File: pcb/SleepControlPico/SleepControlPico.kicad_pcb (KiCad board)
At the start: 2 copper layers, 74.4 x 49.3 mm, 24 parts, among them J1 USB_C_Receptacle_PowerOnly_6P, J3 UART, J4 FFC2B35-18-G_REVA2, SW1 RotaryEncoder_Switch, SW2 SW_Push, U1 AMS1117-33, U2 ESP32-WROOM-32D, U3 LIS3DH

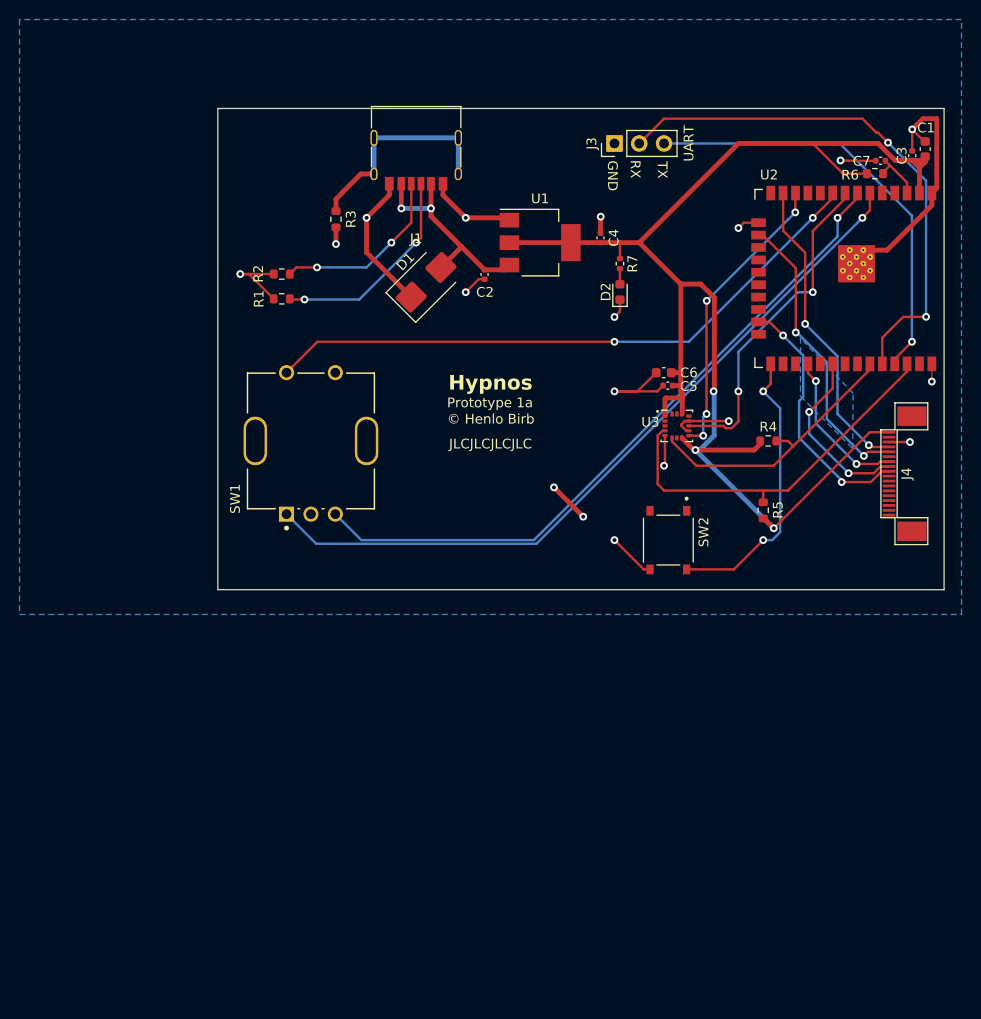
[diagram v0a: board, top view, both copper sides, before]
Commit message: Smaller PCB using an ESP32-S3-MINI-1.
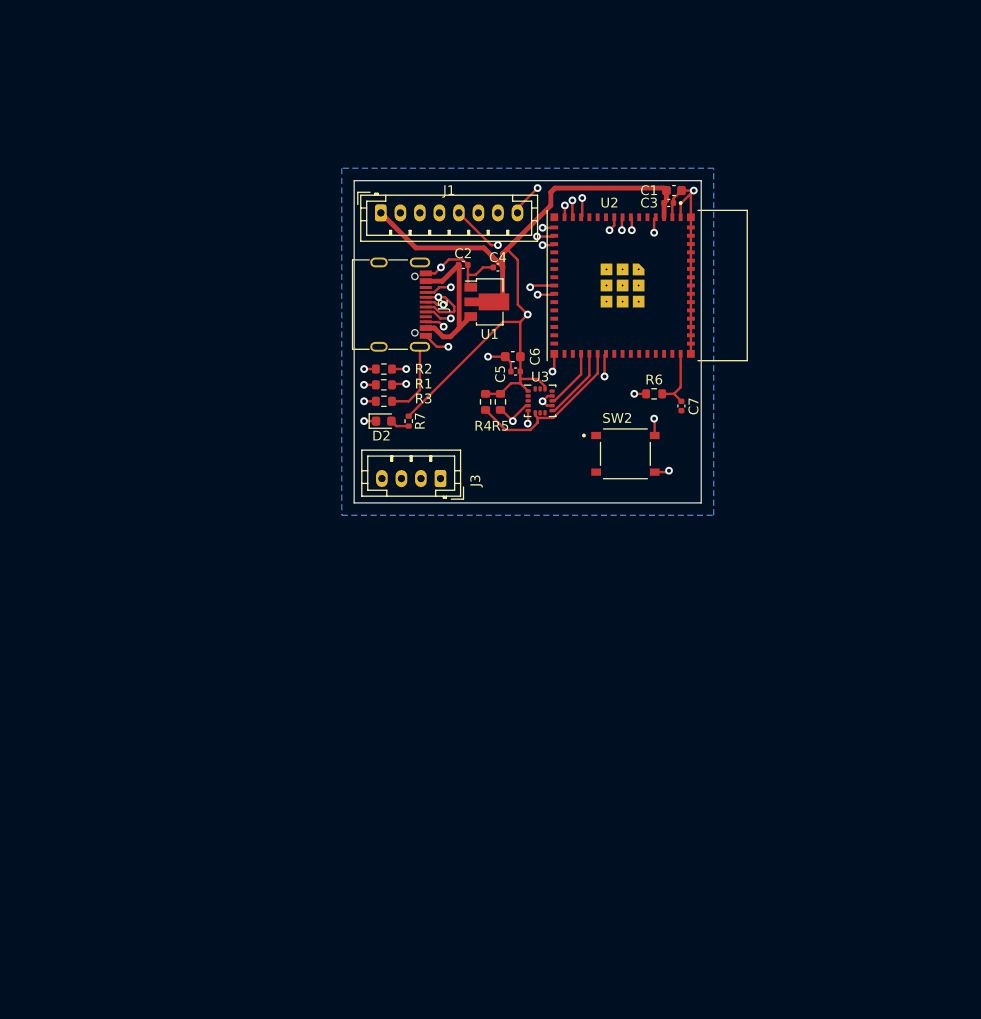
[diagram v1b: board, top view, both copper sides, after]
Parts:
- removed D1: SMBJ6.0A, Diode_SMD:D_SMB
- removed J4: FFC2B35-18-G_REVA2, Connector_FFC-FPC:Jushuo_AFC07_S18FCC
- removed SW1: RotaryEncoder_Switch, eec:Bourns-PEC11R-4020F-S0012-MFG
- added J2: USB_C_Receptacle_USB2.0, Connector_USB:USB_C_Receptacle_G-Switch_GT-USB-7010ASV, F.Cu at (116.6, 64.8)
- J1: value USB_C_Receptacle_PowerOnly_6P -> Conn_01x08_Pin; footprint Connector_USB:USB_C_Receptacle_G-Switch_GT-USB-7002C -> Connector_JST:JST_PH_B8B-PH-K_1x08_P2.00mm_Vertical
- J3: value UART -> Conn_01x04_Socket; footprint Connector_PinHeader_2.54mm:PinHeader_1x03_P2.54mm_Vertical -> Connector_JST:JST_PH_B4B-PH-K_1x04_P2.00mm_Vertical
- U1: footprint Package_TO_SOT_SMD:SOT-223-3_TabPin2 -> Package_TO_SOT_SMD:SOT-89-3
- U2: value ESP32-WROOM-32D -> ESP32-S3-MINI-1-N8; footprint RF_Module:ESP32-WROOM-32D -> ESP32-S3-MINI-1-N8:XCVR_ESP32-S3-MINI-1-N8
- moved J3 38.7 mm to (121.9, 82.6), turned to 180 degrees
- moved C7 32.4 mm to (146.6, 75.2), turned to 90 degrees
- moved R6 32.0 mm to (143.8, 73.9)
- moved R4 29.2 mm to (126.5, 74.7), turned to -90 degrees
- moved R5 29.1 mm to (128.0, 74.7), turned to 90 degrees
- moved D2 27.6 mm to (116.1, 76.7), turned to 0 degrees
- moved R7 27.0 mm to (118.6, 76.7)
- moved C1 26.1 mm to (145.8, 53.1), turned to 0 degrees
- moved C3 25.4 mm to (145.3, 54.4), turned to 0 degrees
- moved U2 23.5 mm to (140.5, 62.8)
- moved R3 19.3 mm to (116.1, 74.7), turned to 180 degrees
- moved C5 15.7 mm to (129.6, 71.6)
- moved C6 15.5 mm to (129.3, 70.1)
- moved R2 14.3 mm to (116.1, 71.4)
- moved U3 14.2 mm to (132.1, 74.6)
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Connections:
- R1 pad 1: Net-(J1-CC1) -> Net-(J2-CC1)
- R2 pad 1: Net-(J1-CC2) -> Net-(J2-CC2)
- R3 pad 1: Net-(J1-SHIELD) -> Net-(J2-SHIELD)
- R4 pad 2: Net-(U2-IO21) -> Net-(U2-IO39)
- U2 pad 12: Net-(U2-IO27) -> unconnected-(U2-IO8-Pad12)
- U2 pad 13: Net-(J4-SCK) -> /Disp_LITE
- U2 pad 14: unconnected-(U2-IO12-Pad14) -> /Disp_RST
- U2 pad 15: GND -> /Disp_MOSI
- U2 pad 16: Net-(J4-MOSI) -> /Disp_SCLK
- U2 pad 17: unconnected-(U2-SHD/SD2-Pad17) -> /Disp_CS
- U2 pad 18: unconnected-(U2-SWP/SD3-Pad18) -> /Disp_DC
- U2 pad 2: +3.3V -> GND
- U2 pad 24: unconnected-(U2-IO2-Pad24) -> Net-(U2-IO20)
- U2 pad 25: Net-(U2-IO0) -> unconnected-(U2-IO21-Pad25)
- U2 pad 28: Net-(J4-DC) -> unconnected-(U2-IO33-Pad28)
- U2 pad 3: Net-(U2-EN) -> +3.3V
- U2 pad 30: Net-(J4-RST) -> unconnected-(U2-IO48-Pad30)
- U2 pad 33: Net-(U2-IO21) -> Net-(U2-IO37)
- U2 pad 34: Net-(J3-Pin_2) -> Net-(U2-IO38)
- U2 pad 35: Net-(J3-Pin_3) -> Net-(U2-IO39)
- U2 pad 38: GND -> unconnected-(U2-IO42-Pad38)
- U2 pad 39: GND -> unconnected-(U2-TXD0-Pad39)
- U2 pad 4: unconnected-(U2-SENSOR_VP-Pad4) -> Net-(U2-IO0)
- U2 pad 6: Net-(U2-IO34) -> unconnected-(U2-IO2-Pad6)
- U2 pad 7: Net-(U2-IO35) -> Net-(J3-Pin_2)
- U2 pad 8: Net-(U2-IO32) -> Net-(J3-Pin_3)
- U2 pad 9: Net-(U2-IO33) -> Net-(J3-Pin_4)
- U3 pad 11: Net-(U2-IO32) -> Net-(U2-IO37)
- U3 pad 6: Net-(U2-IO21) -> Net-(U2-IO39)
- U3 pad 8: +3.3V -> unconnected-(U3-CS-Pad8)
- U3 pad 9: Net-(U2-IO27) -> Net-(U2-IO38)
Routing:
- net Net-(U2-IO34): track 77.0 -> 0.00 mm, vias 1 -> 0
- net Net-(U2-IO35): track 70.7 -> 0.00 mm, vias 1 -> 0
- net Net-(U2-IO33): track 63.9 -> 0.00 mm, vias 2 -> 0
- net GND: track 102.2 -> 53.2 mm, vias 18 -> 12
- net +3.3V: track 145.0 -> 101.4 mm, vias 3 -> 2
- net Net-(J3-Pin_4): track 0.00 -> 36.9 mm, vias 0 -> 1
- net Net-(U2-IO32): track 34.3 -> 0.00 mm, vias 2 -> 0
- net Net-(J4-SCK): track 31.6 -> 0.00 mm, vias 2 -> 0
- net Net-(J4-MOSI): track 30.5 -> 0.00 mm, vias 2 -> 0
- net Net-(U2-IO27): track 30.3 -> 0.00 mm, vias 4 -> 0
- net Net-(U2-IO21): track 28.3 -> 0.00 mm
- net Net-(J2-SHIELD): track 0.00 -> 24.8 mm
- net Net-(J1-SHIELD): track 22.3 -> 0.00 mm
- net Net-(J1-CC1): track 21.6 -> 0.00 mm, vias 2 -> 0
- net Net-(U2-IO40): track 38.8 -> 19.2 mm, vias 0 -> 2
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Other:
- board size 74.4 x 49.3 mm -> 35.6 x 33 mm
- copper layers 2 -> 4
- board text removed: "GND"
- board text removed: "Hypnos"
- board text removed: "JLCJLCJLCJLC"
- board text removed: "Prototype 1a"
- board text removed: "RX"
- board text removed: "TX"
- board text removed: "© Henlo Birb"

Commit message: Final-ish PCB layout
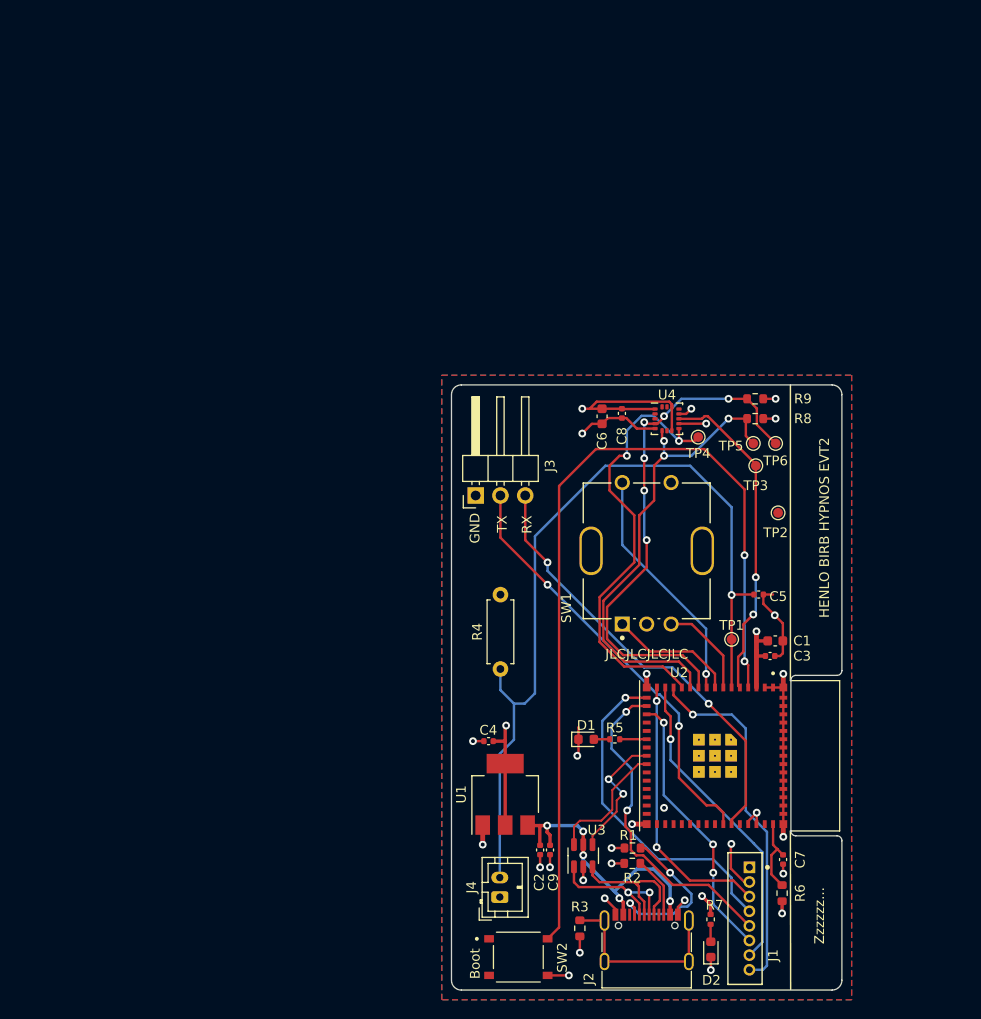
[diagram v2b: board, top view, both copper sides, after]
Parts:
- added C8: 0.1 µF, Capacitor_SMD:C_0402_1005Metric, F.Cu at (140.5, 75.9)
- added C9: 100 nF, Capacitor_SMD:C_0402_1005Metric, F.Cu at (133.1, 120.7)
- added D1: LED, LED_SMD:LED_0603_1608Metric, F.Cu at (136.8, 109.3)
- added J4: Photodiode, Connector_JST:JST_PH_B2B-PH-K_1x02_P2.00mm_Vertical, F.Cu at (128.0, 125.5)
- added R8: 4K7, Resistor_SMD:R_0603_1608Metric, F.Cu at (154.1, 76.5)
- added R9: 4K7, Resistor_SMD:R_0603_1608Metric, F.Cu at (154.1, 74.4)
- added SW1: RotaryEncoder_Switch, eec:Bourns-PEC11R-4020F-S0012-MFG, F.Cu at (143.0, 90.0)
- added TP1: TestPoint, TestPoint:TestPoint_Pad_D1.0mm, F.Cu at (151.7, 99.1)
- added TP2: TestPoint, TestPoint:TestPoint_Pad_D1.0mm, F.Cu at (156.5, 86.1)
- added TP3: TestPoint, TestPoint:TestPoint_Pad_D1.0mm, F.Cu at (154.2, 81.3)
- added TP4: TestPoint, TestPoint:TestPoint_Pad_D1.0mm, F.Cu at (148.3, 78.3)
- added TP5: TestPoint, TestPoint:TestPoint_Pad_D1.0mm, F.Cu at (153.9, 79.0)
- added TP6: TestPoint, TestPoint:TestPoint_Pad_D1.0mm, F.Cu at (156.2, 79.0)
- added U4: LIS3DH, Package_LGA:LGA-16_3x3mm_P0.5mm_LayoutBorder3x5y, F.Cu at (145.1, 76.5)
- C5: value 0.1 µF -> 100 nF
- J1: value Conn_01x08_Pin -> Display; footprint Connector_JST:JST_PH_B8B-PH-K_1x08_P2.00mm_Vertical -> JST B8B-ZR:JST-B8B-ZR-0
- J3: value Conn_01x04_Socket -> Conn_01x03; footprint Connector_JST:JST_PH_B4B-PH-K_1x04_P2.00mm_Vertical -> Connector_PinHeader_2.54mm:PinHeader_1x03_P2.54mm_Horizontal
- R1, R2: value 5.1K -> 5K1
- R4: value 2.2 kΩ -> 200K; footprint Resistor_SMD:R_0603_1608Metric -> Resistor_THT:R_Axial_DIN0207_L6.3mm_D2.5mm_P7.62mm_Horizontal
- R5: value 2.2 kΩ -> 150R; footprint Resistor_SMD:R_0603_1608Metric -> Resistor_SMD:R_0402_1005Metric
- R6: value 10 kΩ -> 10K
- R7: value 75Ω -> 150R
- SW2: value SW_Push -> Boot
- U1: footprint Package_TO_SOT_SMD:SOT-89-3 -> Package_TO_SOT_SMD:SOT-223-3_TabPin2
- U3: value LIS3DH -> USBLC6-2SC6; footprint Package_LGA:LGA-16_3x3mm_P0.5mm_LayoutBorder3x5y -> Package_TO_SOT_SMD:SOT-23-6
- moved J1 81.4 mm to (153.1, 127.7), turned to -90 degrees
- moved J2 71.3 mm to (143.0, 131.0), turned to 0 degrees
- moved D2 63.7 mm to (149.6, 130.8), turned to 90 degrees
- moved C2 60.5 mm to (132.1, 120.7), turned to -90 degrees
- moved R7 59.7 mm to (149.6, 127.8)
- moved R3 57.6 mm to (136.2, 128.7), turned to -90 degrees
- moved R2 56.7 mm to (141.5, 122.0)
- moved R1 53.9 mm to (141.6, 120.5)
- moved R6 52.8 mm to (156.9, 125.1), turned to 90 degrees
- moved SW2 52.7 mm to (129.8, 131.6)
- moved U1 50.5 mm to (128.5, 115.0), turned to 90 degrees
- moved U2 49.1 mm to (150.0, 111.0)
- moved C4 48.5 mm to (126.8, 109.5)
- moved C7 47.6 mm to (157.0, 121.6)
- moved C3 47.6 mm to (155.6, 100.8)
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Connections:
- net Net-(J2-CC1) renamed /CC1
- net Net-(J2-CC2) renamed /CC2
- net Net-(J2-SHIELD) renamed /SHIELD
- net Net-(U2-EN) renamed /EN
- net Net-(U2-IO0) renamed /BOOT
- C5 pad 1: +3.3V -> GND
- C5 pad 2: GND -> /PD-
- C6 pad 1: +3.3V -> GND
- C6 pad 2: GND -> +3.3V
- J2 pad A6: Net-(U2-IO20) -> /USB_D-
- J2 pad A7: Net-(U2-IO19) -> /USB_D+
- J2 pad B6: Net-(U2-IO20) -> /USB_D-
- J2 pad B7: Net-(U2-IO19) -> /USB_D+
- J3 pad 2: Net-(J3-Pin_2) -> /UART_TX
- J3 pad 3: Net-(J3-Pin_3) -> /UART_RX
- R4 pad 1: +3.3V -> /PD-
- R4 pad 2: Net-(U2-IO39) -> GND
- R5 pad 1: Net-(U2-IO40) -> Net-(D1-A)
- R5 pad 2: +3.3V -> /Status_LED
- U2 pad 10: unconnected-(U2-IO6-Pad10) -> /ACC_SCL
- U2 pad 11: unconnected-(U2-IO7-Pad11) -> /ACC_SDA
- U2 pad 12: unconnected-(U2-IO8-Pad12) -> /ACC_INT2
- U2 pad 21: unconnected-(U2-IO17-Pad21) -> /Status_LED
- U2 pad 33: Net-(U2-IO37) -> unconnected-(U2-IO37-Pad33)
- U2 pad 34: Net-(U2-IO38) -> unconnected-(U2-IO38-Pad34)
- U2 pad 35: Net-(U2-IO39) -> unconnected-(U2-IO39-Pad35)
- U2 pad 36: Net-(U2-IO40) -> unconnected-(U2-IO40-Pad36)
- U2 pad 39: unconnected-(U2-TXD0-Pad39) -> /UART_TX
- U2 pad 40: unconnected-(U2-RXD0-Pad40) -> /UART_RX
- U2 pad 5: unconnected-(U2-IO1-Pad5) -> /ACC_INT1
- U2 pad 6: unconnected-(U2-IO2-Pad6) -> /PD-
- U2 pad 7: Net-(J3-Pin_2) -> /ROTARY_B
- U2 pad 8: Net-(J3-Pin_3) -> /ROTARY_A
- U2 pad 9: Net-(J3-Pin_4) -> /ROTARY_S
- U3 pad 1: +3.3V -> /USB_D+
- U3 pad 2: unconnected-(U3-NC-Pad2) -> GND
- U3 pad 3: unconnected-(U3-NC-Pad3) -> /USB_D-
- U3 pad 4: Net-(U2-IO40) -> Net-(U2-IO19)
- U3 pad 5: GND -> +5V
- U3 pad 6: Net-(U2-IO39) -> Net-(U2-IO20)
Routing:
- net /PD-: track 0.00 -> 86.9 mm, vias 0 -> 1
- net /BOOT: track 22.5 -> 89.6 mm
- net +3.3V: track 101.4 -> 44.3 mm, vias 2 -> 7
- net /ACC_SCL: track 0.00 -> 53.9 mm, vias 0 -> 6
- net /ACC_SDA: track 0.00 -> 48.9 mm, vias 0 -> 3
- net /ACC_INT2: track 0.00 -> 46.3 mm, vias 0 -> 2
- net /UART_RX: track 0.00 -> 45.3 mm, vias 0 -> 2
- net /UART_TX: track 0.00 -> 43.9 mm, vias 0 -> 2
- net Net-(J3-Pin_4): track 36.9 -> 0.00 mm, vias 1 -> 0
- net Net-(J3-Pin_2): track 36.5 -> 0.00 mm, vias 1 -> 0
- net Net-(J3-Pin_3): track 36.2 -> 0.00 mm, vias 1 -> 0
- net /ACC_INT1: track 0.00 -> 33.7 mm, vias 0 -> 2
- net /Disp_LITE: track 10.4 -> 36.8 mm, vias 2 -> 1
- net /ROTARY_S: track 0.00 -> 24.6 mm, vias 0 -> 1
- net /Disp_CS: track 11.6 -> 33.8 mm
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- added copper zone on In2.Cu, net +3.3V
- added copper zone on F.Cu, net GND
- added copper zone on In1.Cu, net GND
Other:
- board size 35.6 x 33 mm -> 40 x 62 mm
- board text added: "GND"
- board text added: "HENLO BIRB HYPNOS EVT2"
- board text added: "JLCJLCJLCJLC"
- board text added: "RX"
- board text added: "TX"
- board text added: "Zzzzzz..."

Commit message: remove accelerometer (out of stock)
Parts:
- removed C6: 10 µF, Capacitor_SMD:C_0603_1608Metric
- removed C8: 0.1 µF, Capacitor_SMD:C_0402_1005Metric
- removed R8, R9: 4K7, Resistor_SMD:R_0603_1608Metric
- removed TP3, TP4, TP5, TP6: TestPoint, TestPoint:TestPoint_Pad_D1.0mm
- removed U4: LIS3DH, Package_LGA:LGA-16_3x3mm_P0.5mm_LayoutBorder3x5y
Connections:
- U2 pad 10: /ACC_SCL -> unconnected-(U2-IO6-Pad10)
- U2 pad 11: /ACC_SDA -> unconnected-(U2-IO7-Pad11)
- U2 pad 12: /ACC_INT2 -> unconnected-(U2-IO8-Pad12)
- U2 pad 5: /ACC_INT1 -> unconnected-(U2-IO1-Pad5)
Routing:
- net /ACC_SCL: track 53.9 -> 0.00 mm, vias 6 -> 0
- net /ACC_SDA: track 48.9 -> 0.00 mm, vias 3 -> 0
- net /ACC_INT2: track 46.3 -> 0.00 mm, vias 2 -> 0
- net /ACC_INT1: track 33.7 -> 0.00 mm, vias 2 -> 0
- net +3.3V: track 44.3 -> 22.8 mm, vias 7 -> 4
- net GND: track 73.6 -> 60.7 mm, vias 25 -> 22

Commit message: Final(?) PCB revision.
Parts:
- moved J2 0.50 mm to (143.0, 131.5)
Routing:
- net /USB_D+: track 14.8 -> 15.8 mm
- net GND: track 60.7 -> 61.7 mm
- net /USB_D-: track 15.0 -> 16.0 mm
- net +5V: track 30.7 -> 31.7 mm
- net /CC2: track 6.30 -> 6.81 mm
- net /CC1: track 16.7 -> 17.2 mm
